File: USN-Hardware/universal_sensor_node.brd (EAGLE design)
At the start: 23.9 x 26.7 mm, 26 parts, among them IC2 741G3157DCKR, IC3 AP2114, J2 USB-MICROB, U1 ATMEGA328P_TQFP

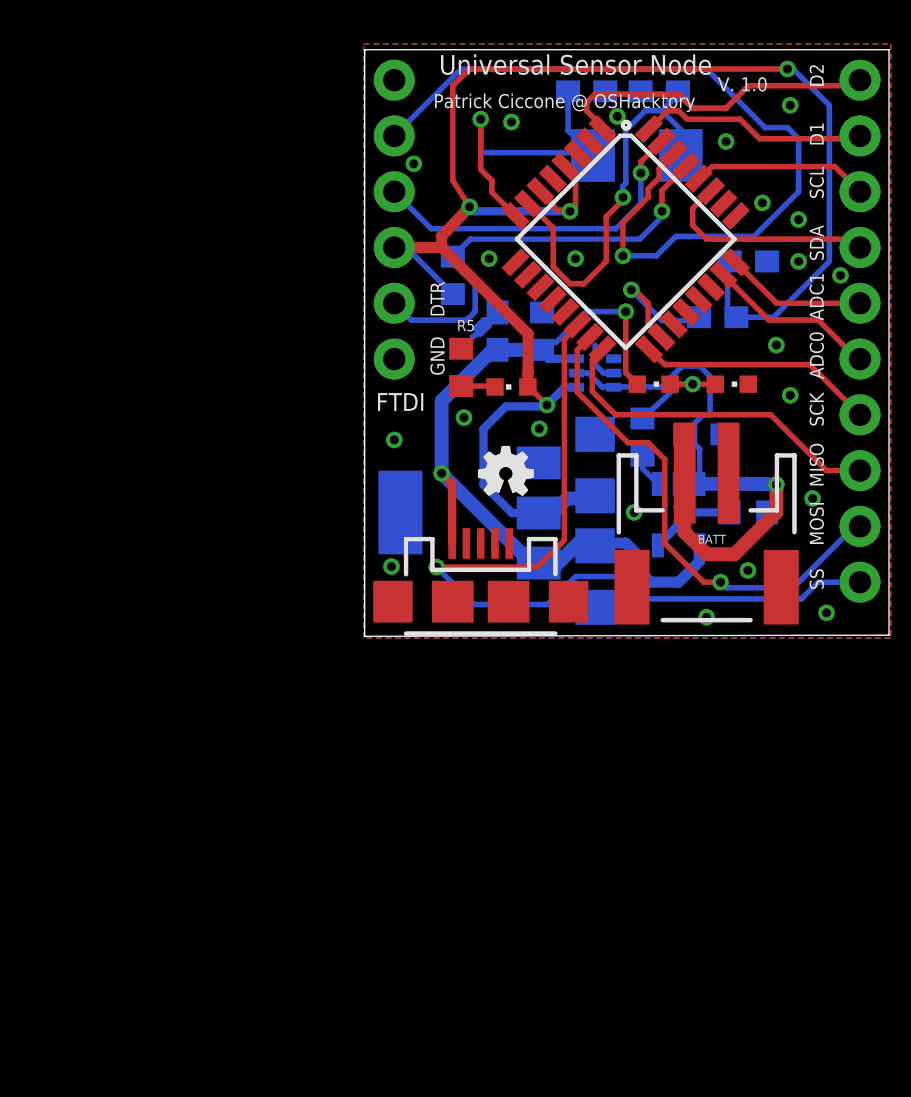
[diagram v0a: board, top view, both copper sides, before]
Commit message: converting all parts into schematic library.
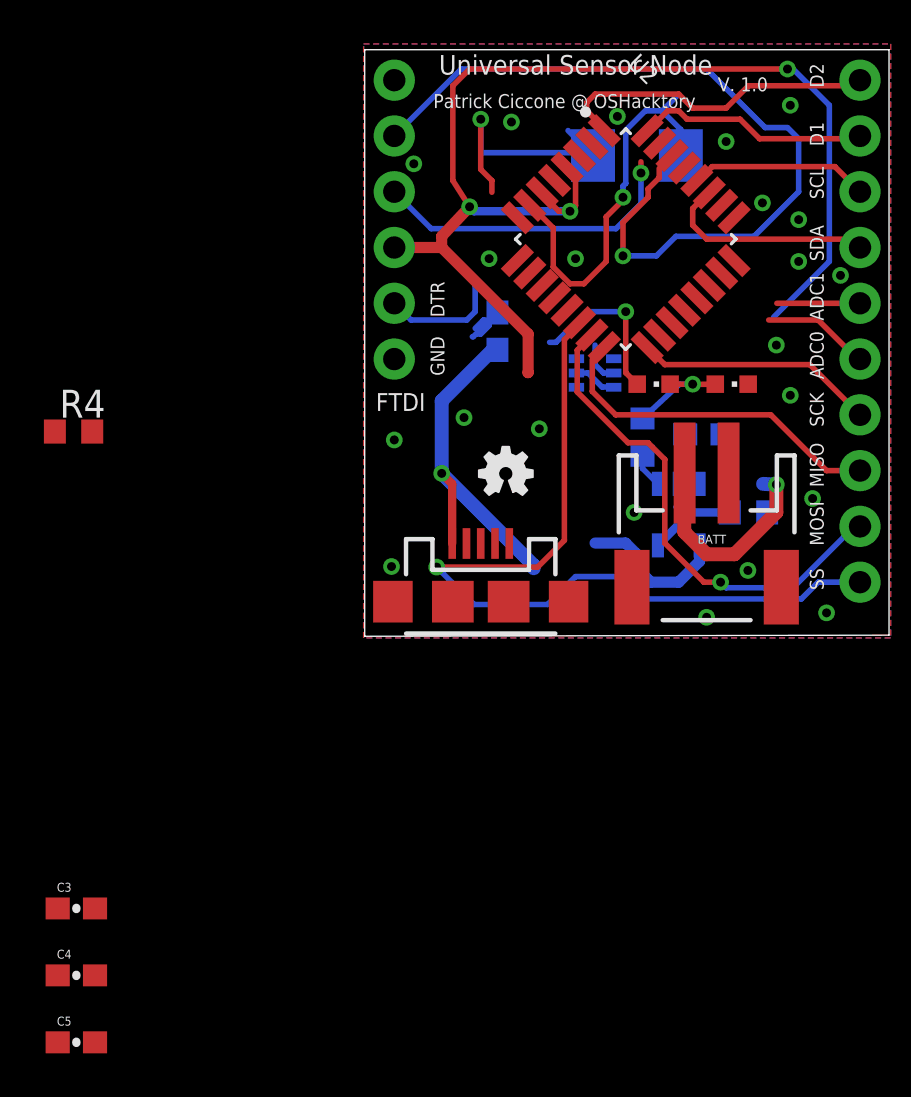
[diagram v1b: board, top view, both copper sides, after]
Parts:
- removed C6, C7: 22pF, rcl:C0603
- removed GREEN: PWR, led:CHIPLED_0603
- removed IC3: AP2114, burr-brown:SOT223
- removed L1: 10uH, SparkFun-Passives:0603
- removed R1: 10k, rcl:R0603
- removed R5: 1k, rcl:R0603
- removed U1: ATMEGA328P_TQFP, SparkFun-DigitalIC:TQFP32-08
- added U2: ATMEGA328PB-AU, ATMEGA328PB-AU:QFP80P900X900X120-32N
- C3: value 4.7uF -> 100nF; device rcl:C1206 -> universal_sensor_node:0603-CAP
- C4: value 4.7uF -> 22pF; device rcl:C1206 -> universal_sensor_node:0603-CAP
- C5: value 100nF -> 22pF; device rcl:C0603 -> universal_sensor_node:0603-CAP
- moved C5 46.9 mm to (-12.8, -18.4), flipped to the top, turned to 0 degrees
- moved C4 33.1 mm to (-12.8, -15.4), flipped to the top, turned to 0 degrees
- moved C3 28.0 mm to (-12.8, -12.3), flipped to the top, turned to 0 degrees
- moved R4 18.7 mm to (-13.0, 9.40), flipped to the top, turned to 0 degrees
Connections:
- removed net ASDF: L1.1, U1.18
- removed net HIGH: IC2.1
- removed net N$28: C7.1, U1.7, X1.P$2
- removed net N$29: C6.1, U1.8, X1.P$1
- removed net N$5: GREEN.C, R5.1
- new net N$26: C4.2, U2.7, X1.P$2
- new net N$27: C5.2, U2.8, X1.P$1
- new net NC13: U2.3
- new net NC14: U2.6
- net 3V7: now also C3.1, R4.1, U2.18, U2.4; no longer C4.1, C5.1, GREEN.A, IC2.4, IC3.2, L1.2, R4.2, U1.4, U1.6
- net 5V: no longer C3.1, IC2.6, IC3.3, R1.2
- net ADC0: now also U2.23; no longer U1.23
- net ADC1: now also U2.24; no longer U1.24
- net D1: now also U2.32; no longer U1.32
- net D2: now also U2.1; no longer U1.1
- net DTR: now also R4.2, U2.29; no longer R4.1, U1.29
- net GND: now also C4.1, C5.1, U2.21, U2.5; no longer C4.2, C5.2, C6.2, C7.2, IC3.1, R1.1, R5.2, U1.21, U1.3, U1.5
- net MISO: now also U2.16; no longer U1.16
- net MOSI: now also U2.15; no longer U1.15
- net NC1: now also U2.20; no longer U1.20
- net NC10: now also U2.22; no longer U1.22
- net NC11: now also U2.25; no longer U1.25
- net NC12: now also U2.26; no longer U1.26
- net NC3: now also U2.2; no longer U1.2
- net NC4: now also U2.9; no longer U1.9
- net NC5: now also U2.10; no longer U1.10
- net NC6: now also U2.11; no longer U1.11
- net NC7: now also U2.12; no longer U1.12
- net NC8: now also U2.13; no longer U1.13
- net NC9: now also U2.19; no longer U1.19
- net RX: now also U2.30; no longer U1.30
- net SCK: now also U2.17; no longer U1.17
- net SCL: now also U2.28; no longer U1.28
- net SDA: now also U2.27; no longer U1.27
- net SS: now also U2.14; no longer U1.14
- net TX: now also U2.31; no longer U1.31
- net VBATT: no longer IC2.3
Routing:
- net 3V7: track 79.5 -> 55.9 mm, vias 4 -> 3
- net N$28: track 18.5 -> 0.00 mm, vias 1 -> 0
- net N$26: track 0.00 -> 18.3 mm, vias 0 -> 1
- net N$29: track 14.8 -> 0.00 mm, vias 1 -> 0
- net VBATT: track 25.6 -> 11.9 mm
- net DTR: track 20.1 -> 6.99 mm, vias 1 -> 0
- net N$27: track 0.00 -> 11.5 mm, vias 0 -> 1
- net 5V: track 39.1 -> 31.0 mm
- net ASDF: track 6.52 -> 0.00 mm, vias 1 -> 0
- net ADC0: track 7.81 -> 4.89 mm
- net ADC1: track 6.43 -> 3.79 mm
- net N$5: track 1.58 -> 0.00 mm
- net TX: track 15.6 -> 14.3 mm
- net RX: track 38.2 -> 37.3 mm
- net MISO: track 15.8 -> 15.1 mm

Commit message: finished with atmega components transfer.
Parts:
- removed R4: 10k, rcl:R0603
- removed X1: (no value), adafruit:NX5032
- added R1: 10k, universal_sensor_node:0603-RES
- added Y1: TSX-3225EPSON_TSX-3225_16.0000MF09Z-AC3_0_0, universal_sensor_node:TSX-3225
- C4, C5: value 22pF -> 9pF
- moved C4 5.97 mm to (-18.8, -15.4)
- moved C5 5.97 mm to (-18.8, -18.4)
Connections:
- new net N$4: C5.2, Y1.4
- net 3V7: now also R1.1; no longer R4.1
- net DTR: now also R1.2; no longer R4.2
- net GND: now also C4.2, Y1.2; no longer C4.1, C5.1
- net N$26: now also C4.1, Y1.1; no longer C4.2, X1.P$2
- net N$27: now also C5.1, Y1.3; no longer C5.2, X1.P$1
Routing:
- net N$26: track 18.3 -> 0.00 mm, vias 1 -> 0
- net N$27: track 11.5 -> 0.00 mm, vias 1 -> 0

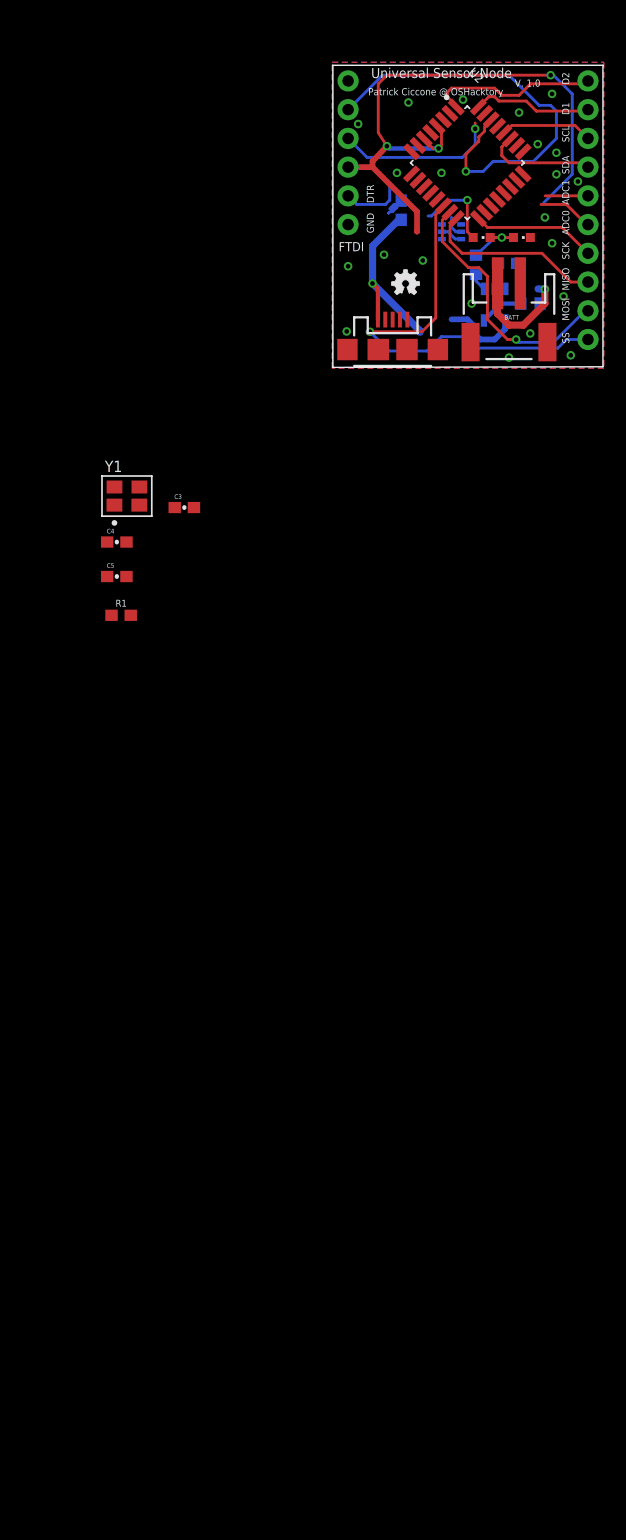
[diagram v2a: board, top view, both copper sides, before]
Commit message: copied all all schematic components to project library.  Cleaned up schematic.
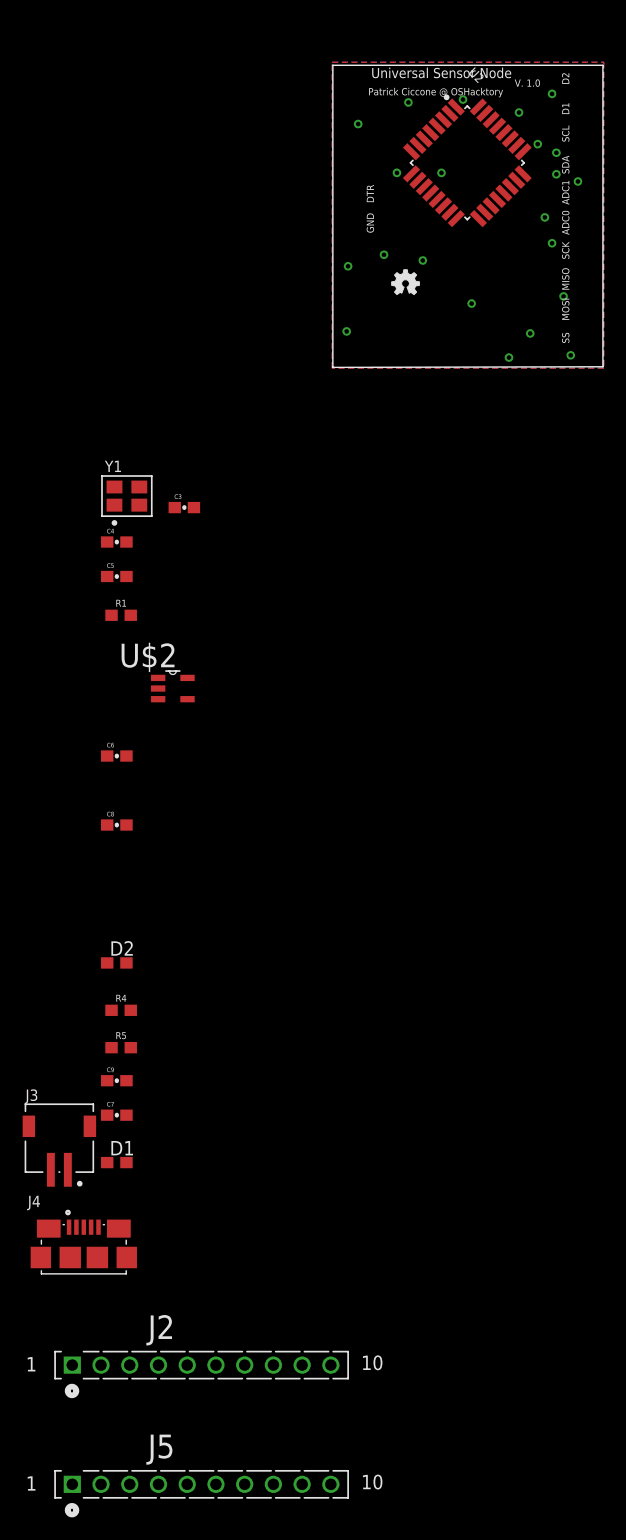
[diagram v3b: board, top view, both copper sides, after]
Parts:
- removed BATT: (no value), SparkFun-Connectors:JST-2-SMD
- removed BLUE: FULL, led:CHIPLED_0603
- removed C1, C2: 4.7uF, rcl:C0603
- removed FTDI: (no value), SparkFun-Connectors:1X06_NO_SILK
- removed IC2: 741G3157DCKR, 74xx-little-de:DCK_R-PDSO-G6
- removed J1: (no value), SparkFun-Connectors:1X10_NO_SILK
- removed R2: 6.7k-10k, rcl:R0603
- removed R3: 1k, rcl:R0603
- removed U$1: MCP73831, GeekAmmo:SOT23-5
- removed YELLOW: CHRG, led:CHIPLED_0603
- added C6, C7: 10uF, universal_sensor_node:0603-CAP
- added C8, C9: 0.1uF, universal_sensor_node:0603-CAP
- added D1: Yellow, universal_sensor_node:0603
- added D2: Blue, universal_sensor_node:0603
- added J3: JST_S2B-ZR-SM4A-TF_LF_SNJST_S2B-ZR-SM4A-TF_LF_SN_0_0, universal_sensor_node:JST_S2B-ZR-SM4A-TF_LF_SN_0
- added J4: 10118192-0001LF, universal_sensor_node:AMPHENOL_10118192-0001LF
- added J5: SSQ-110-03-T-S, universal_sensor_node:SAMTEC_SSQ-110-03-T-S
- added R4: 1K, universal_sensor_node:0603-RES
- added R5: 6K8, universal_sensor_node:0603-RES
- added U$2: MCP73831T-2ACI/OT, universal_sensor_node:SOT95P280X145-5N
- J2: value USB-MICROB -> SSQ-110-03-T-S; device SparkFun-Connectors:USB-MICROB -> universal_sensor_node:SAMTEC_SSQ-110-03-T-S
- moved J2 90.0 mm to (0.13, -88.1)
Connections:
- removed net N$1: R3.1, U$1.1
- removed net N$2: BLUE.A, R3.2, YELLOW.C
- removed net N$82: R2.2, U$1.5
- removed net NC11: U2.25
- removed net NC3: U2.2
- new net ADC2: J2.4, U2.25
- new net D3: J2.9, U2.2
- new net N$10: R4.1, U$2.1
- new net N$11: D1.1, D2.2, R4.2
- new net N$3: R5.2, U$2.5
- net 3V7: now also J2.1, J5.1; no longer FTDI.4
- net 5V: now also C7.1, C9.1, D1.2, J4.1, U$2.4; no longer C2.1, J2.VBUS, U$1.4, YELLOW.A
- net ADC0: now also J2.2; no longer J1.6
- net ADC1: now also J2.3; no longer J1.5
- net D1: now also J2.7; no longer J1.2
- net D2: now also J2.8; no longer J1.1
- net DTR: now also J5.2; no longer FTDI.5
- net GND: now also C6.2, C7.2, C8.2, C9.2, D2.1, J2.10, J3.1, J4.5, J5.10, R5.1, U$2.2; no longer BATT.1, BLUE.C, C1.2, C2.2, FTDI.6, IC2.2, J2.GND, J2.MT1, J2.MT2, R2.1, U$1.2
- net MISO: now also J5.7; no longer J1.8
- net MOSI: now also J5.8; no longer J1.9
- net NC2: now also J5.5; no longer FTDI.1
- net RX: now also J5.4; no longer FTDI.2
- net SCK: now also J5.6; no longer J1.7
- net SCL: now also J2.5; no longer J1.3
- net SDA: now also J2.6; no longer J1.4
- net SS: now also J5.9; no longer J1.10
- net TX: now also J5.3; no longer FTDI.3
- net VBATT: now also C6.1, C8.1, J3.2, U$2.3; no longer BATT.2, C1.1, IC2.5, U$1.3
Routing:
- net 3V7: track 55.9 -> 0.00 mm, vias 3 -> 0
- net SS: track 37.6 -> 0.00 mm, vias 1 -> 0
- net RX: track 37.3 -> 0.00 mm, vias 1 -> 0
- net 5V: track 31.0 -> 0.00 mm, vias 2 -> 0
- net MOSI: track 22.7 -> 0.00 mm, vias 1 -> 0
- net MISO: track 15.1 -> 0.00 mm
- net D2: track 14.8 -> 0.00 mm
- net TX: track 14.3 -> 0.00 mm, vias 1 -> 0
- net VBATT: track 11.9 -> 0.00 mm, vias 1 -> 0
- net SCK: track 10.8 -> 0.00 mm
- net D1: track 10.5 -> 0.00 mm
- net SDA: track 9.92 -> 0.00 mm
- net SCL: track 7.98 -> 0.00 mm
- net DTR: track 6.99 -> 0.00 mm
- net GND: track 6.52 -> 0.00 mm
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
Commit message: schematic capture done, board layout done, and everything is routed.
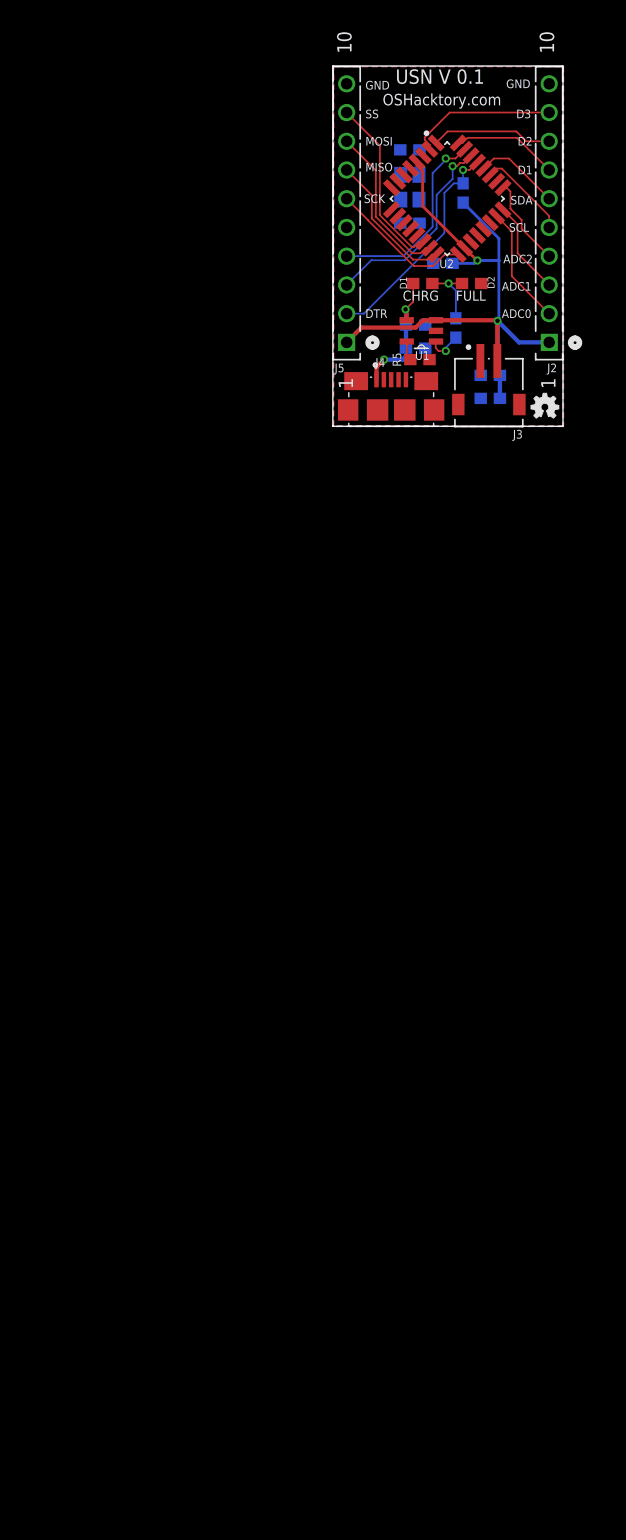
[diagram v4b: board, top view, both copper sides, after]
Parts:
- removed U$2: MCP73831T-2ACI/OT, universal_sensor_node:SOT95P280X145-5N
- added U1: MCP73831T-2ACI/OT, universal_sensor_node:SOT95P280X145-5N
- moved J5 123.8 mm to (1.52, 25.1), turned to 90 degrees
- moved J2 114.9 mm to (19.4, 25.1), turned to 90 degrees
- moved D1 82.3 mm to (8.26, 7.49), turned to 180 degrees
- moved J4 79.7 mm to (5.46, -1.02)
- moved J3 76.1 mm to (14.1, -2.16), turned to 180 degrees
- moved C7 72.8 mm to (7.62, 1.78), flipped to the bottom, turned to 180 degrees
- moved C9 71.8 mm to (7.62, 3.81), flipped to the bottom, turned to 180 degrees
- moved D2 67.8 mm to (12.6, 7.49), turned to 180 degrees
- moved R4 67.2 mm to (11.2, 3.56), flipped to the bottom, turned to 90 degrees
- moved R5 66.3 mm to (8.00, 0.76), turned to 180 degrees
- moved C8 51.7 mm to (14.2, -0.64), flipped to the bottom
- moved R1 48.0 mm to (11.8, 15.5), flipped to the bottom, turned to 90 degrees
- moved C6 45.7 mm to (14.2, -2.67), flipped to the bottom
- moved C4 43.3 mm to (7.11, 19.3), flipped to the bottom
- moved C5 40.6 mm to (7.11, 12.8), flipped to the bottom, turned to 180 degrees
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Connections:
- removed net N$3: R5.2, U$2.5
- removed net N$4: C5.2, Y1.4
- removed net VBATT: C6.1, C8.1, J3.2, U$2.3
- new net STAT: R4.1, U1.1
- net 3V7: now also C6.1, C8.1, J3.2, U1.3
- net 5V: now also U1.4; no longer U$2.4
- net GND: now also C5.2, U1.2, Y1.4; no longer U$2.2
- net N$10: now also R5.2, U1.5; no longer R4.1, U$2.1
- net RX: now also J5.3; no longer J5.4
- net SCL: now also J2.6; no longer J2.5
- net SDA: now also J2.5; no longer J2.6
- net TX: now also J5.4; no longer J5.3
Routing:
- net 3V7: track 0.00 -> 57.1 mm, vias 0 -> 2
- net DTR: track 0.00 -> 19.9 mm, vias 0 -> 1
- net RX: track 0.00 -> 18.1 mm, vias 0 -> 1
- net TX: track 0.00 -> 17.2 mm, vias 0 -> 1
- net SS: track 0.00 -> 15.5 mm
- net MOSI: track 0.00 -> 14.0 mm
- net D3: track 0.00 -> 13.1 mm
- net SCK: track 0.00 -> 12.8 mm
- net MISO: track 0.00 -> 12.6 mm
- net 5V: track 0.00 -> 11.9 mm, vias 0 -> 2
- net D2: track 0.00 -> 10.8 mm
- net ADC0: track 0.00 -> 10.5 mm
- net D1: track 0.00 -> 9.40 mm
- net ADC1: track 0.00 -> 8.33 mm
- net SDA: track 0.00 -> 8.20 mm
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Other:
- board size 23.9 x 26.7 mm -> 20.3 x 31.9 mm
- board text added: "ADC2"
- board text added: "CHRG"
- board text added: "D3"
- board text added: "FULL"
- board text added: "OSHacktory.com"
- board text added: "USN V 0.1"
- board text removed: "Patrick Ciccone @ OSHacktory"
- board text removed: "Universal Sensor Node"
- board text removed: "V. 1.0"
